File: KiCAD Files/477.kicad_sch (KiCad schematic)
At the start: 25 parts, among them IC1 W25N01GVSFIG, IC2 W25N01GVSFIG, IC3 W25N01GVSFIG, IC4 W25N01GVSFIG, J1 BM06B-SRSS-TBT_LF__SN_, J2 6364372-2

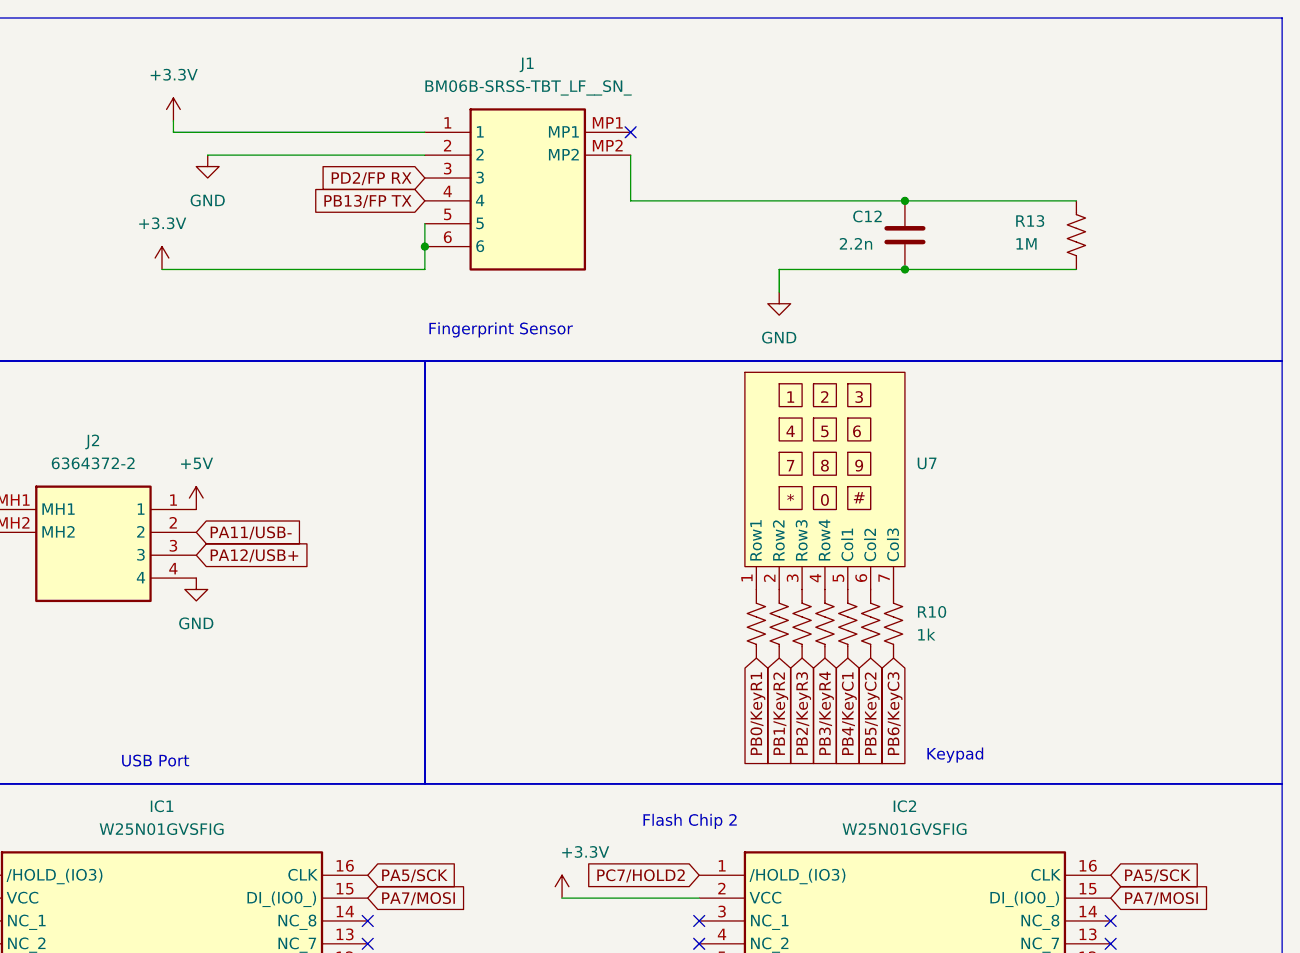
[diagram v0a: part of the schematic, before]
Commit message: added additional connector
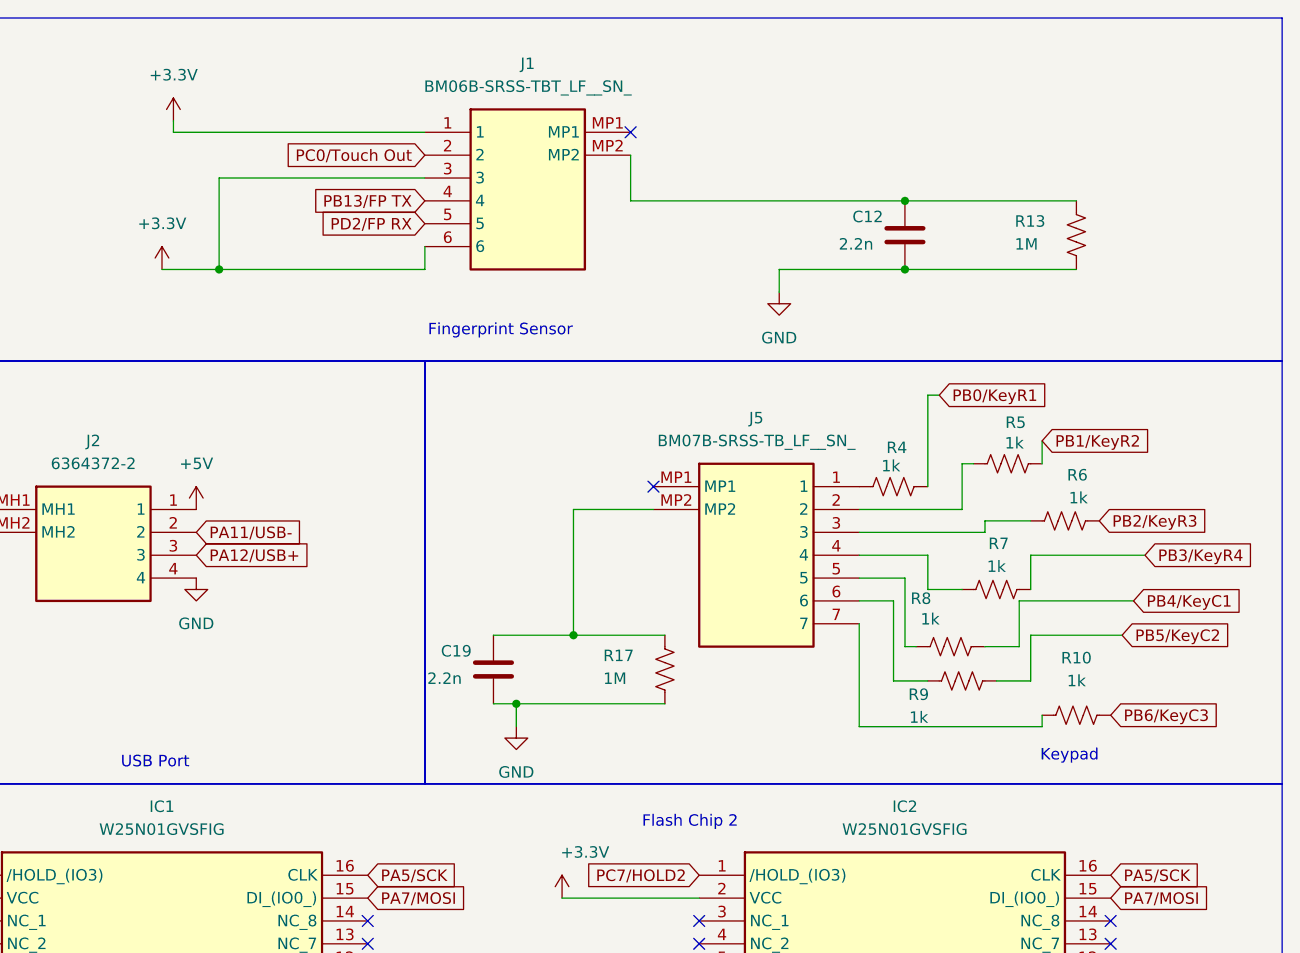
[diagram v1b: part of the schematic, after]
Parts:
- removed U7: ~, symbol CustomSymbols:keypad
- added C19: 2.2n, Capacitor_SMD:C_0805_2012Metric_Pad1.18x1.45mm_HandSolder, symbol CustomSymbols:C
- added J5: BM07B-SRSS-TB_LF__SN_, BM07BSRSSTBLFSN, symbol CustomSymbols:BM07B-SRSS-TB_LF__SN_
- added R17: 1M, Resistor_SMD:R_0805_2012Metric_Pad1.20x1.40mm_HandSolder, symbol CustomSymbols:R_US
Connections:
- net +3.3V: now also J1.3; no longer J1.5
- net GND: now also C19.2, R17.2; no longer J1.2
- net PB3/KeyR4: now also R7.1; no longer R7.2
- net PB4/KeyC1: now also R8.1; no longer R8.2
- net PB6/KeyC3: now also R10.1; no longer R10.2
- net PD2/FP RX: now also J1.5; no longer J1.3
- net at R6.1: now also J5.3
- net at R4.1: now also J5.1
- net at R5.1: now also J5.2
- net at R9.1: now also J5.6
- new net: C19.1, J5.MP2, R17.1
- new net: J5.4, R7.2
- new net: J5.5, R8.2
- new net: J5.7, R10.2
- new net PC0/Touch Out: J1.2
- no-connect marks 44 -> 45

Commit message: found final connector
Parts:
- removed DS1: WC1602A, Display:WC1602A, symbol CustomSymbols:WC1602A
- removed R12: R_US, Resistor_SMD:R_0805_2012Metric_Pad1.20x1.40mm_HandSolder, symbol CustomSymbols:R_US
- added C20: 2.2n, Capacitor_SMD:C_0805_2012Metric_Pad1.18x1.45mm_HandSolder, symbol CustomSymbols:C
- added J6: BM09B-SRSS-TB_LF__SN_, BM09BSRSSTBLFSN, symbol CustomSymbols:BM09B-SRSS-TB_LF__SN_
- R11: value R_US -> 1M
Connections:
- net +3.3V: no longer R11.1
- net +5V: now also J6.3, J6.9
- net GND: now also R11.2, C20.2, J6.1, J6.2, J6.8
- net PB10/LCD SCK: now also J6.6
- net PB12/LCD NSS: now also J6.4
- net PC1/LCD MOSI: now also J6.7
- new net: C20.1, J6.MP2, R11.1
- no-connect marks 45 -> 37
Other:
- note removed: "Revisit with specifications on LCD after part selection."

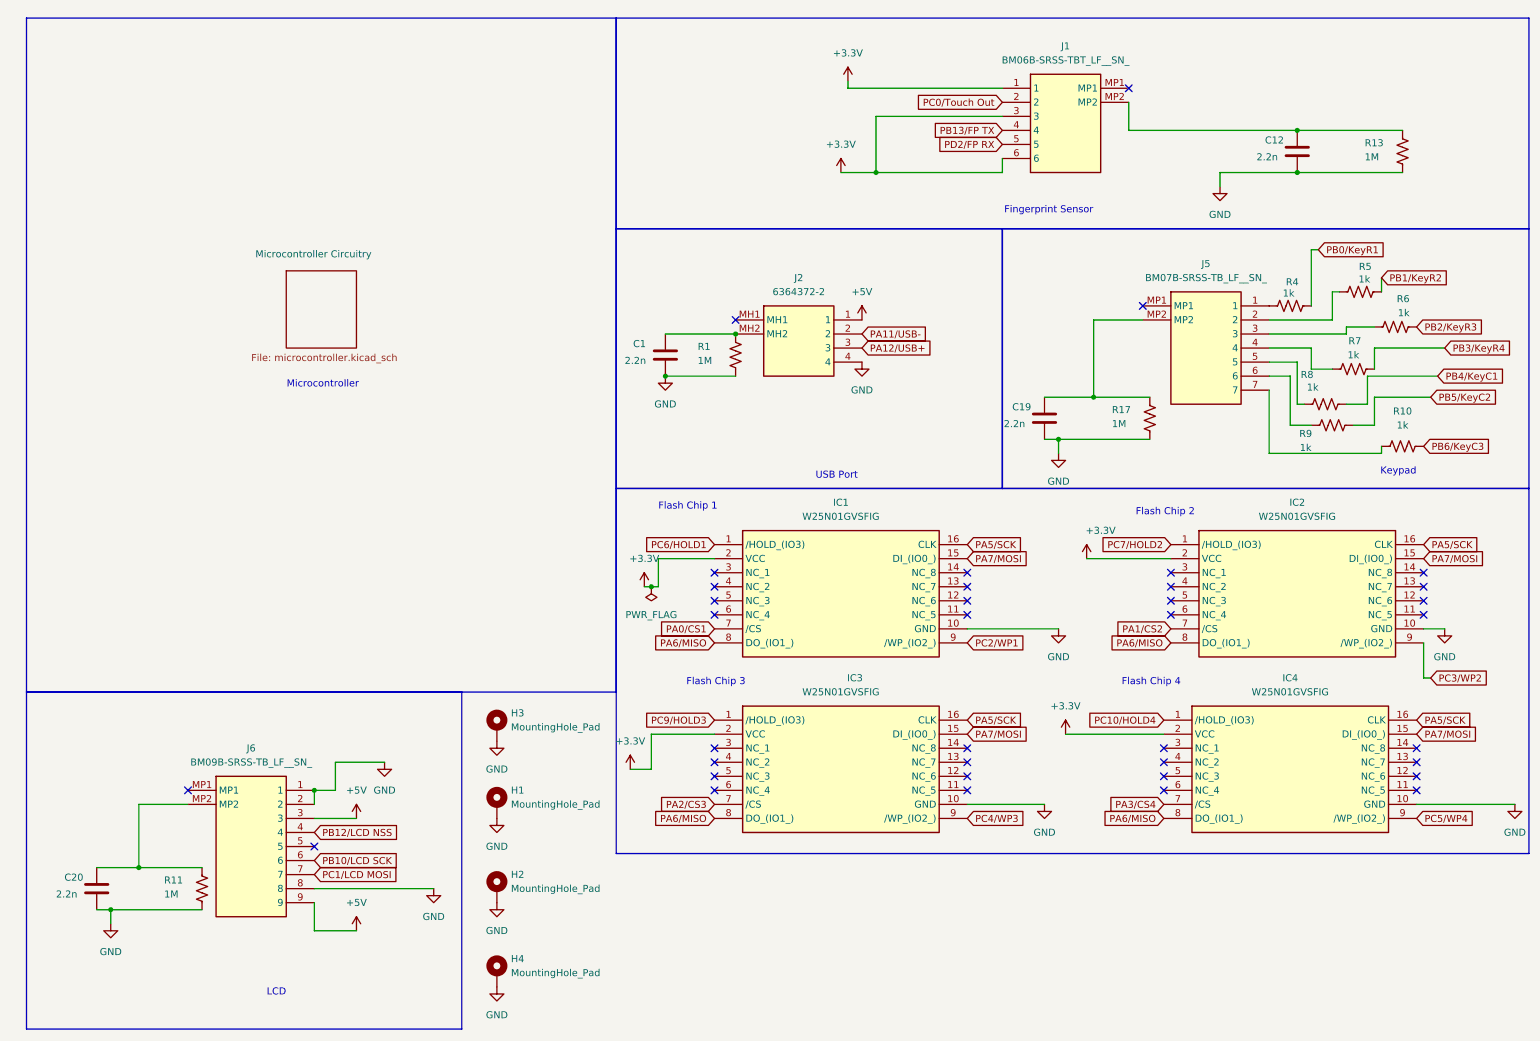
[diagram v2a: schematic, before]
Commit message: finalized schematic
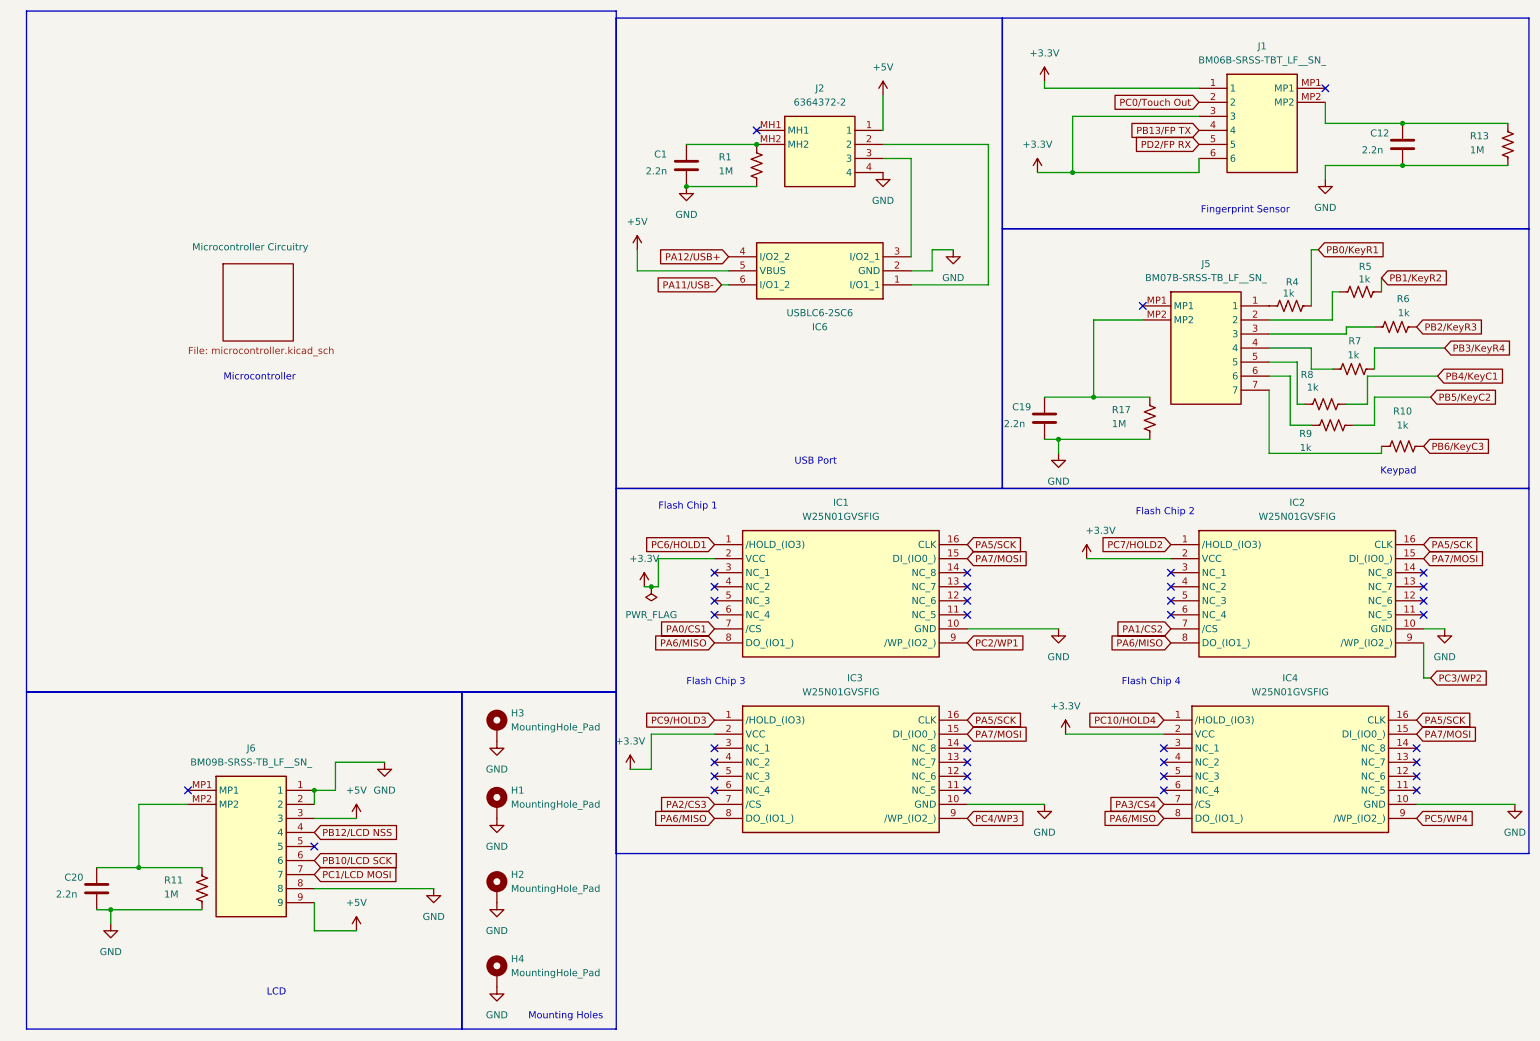
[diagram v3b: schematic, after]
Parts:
- added IC6: USBLC6-2SC6, SOT95P280X145-6N, symbol CustomSymbols:USBLC6-2SC6
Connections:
- net +5V: now also IC6.5 (VBUS)
- net GND: now also IC6.2 (GND)
- net PA11/USB-: now also IC6.6 (I/O1_2); no longer J2.2
- net PA12/USB+: now also IC6.4 (I/O2_2); no longer J2.3
- new net: IC6.1 (I/O1_1), J2.2
- new net: IC6.3 (I/O2_1), J2.3
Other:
- note added: "Mounting Holes"
- moved on the sheet: C1, C12, J1, J2, R1, R13

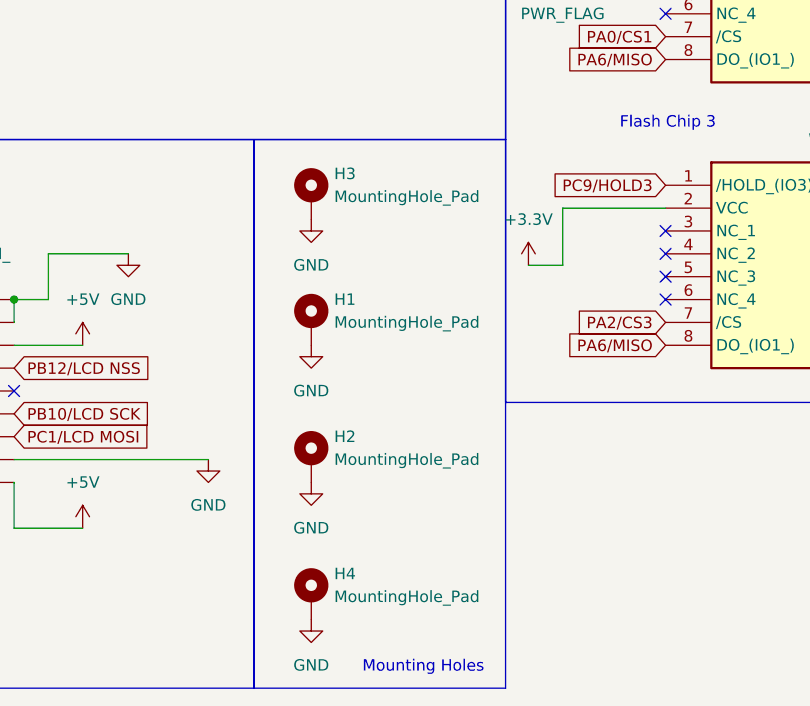
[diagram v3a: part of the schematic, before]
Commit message: modified mounting holes
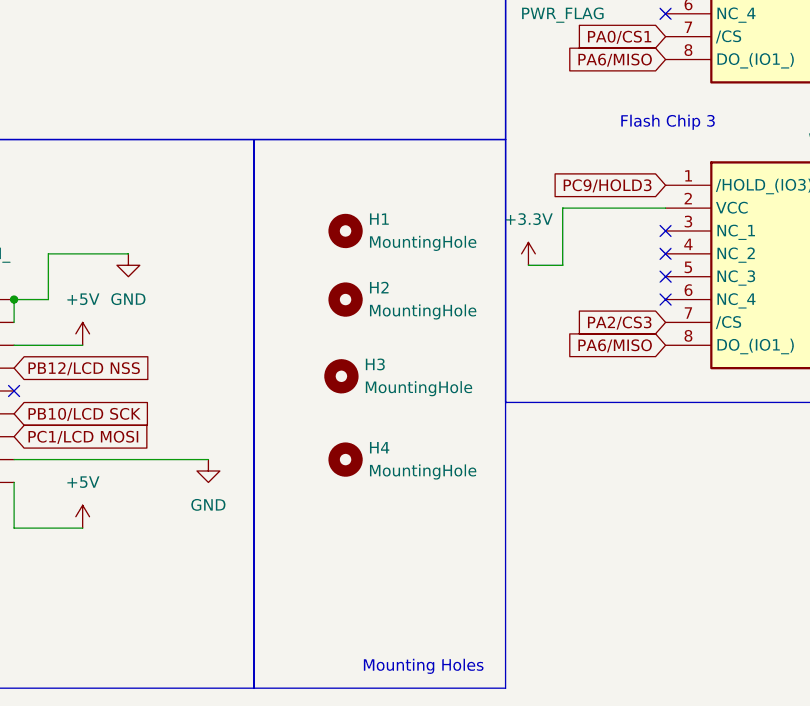
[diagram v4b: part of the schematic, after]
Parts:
- removed H1, H2, H3, H4: MountingHole_Pad, MountingHole:MountingHole_3.2mm_M3_DIN965_Pad, symbol Mechanical:MountingHole_Pad
- added H1, H2, H3, H4: MountingHole, MountingHole:MountingHole_3.2mm_M3_DIN965, symbol Mechanical:MountingHole

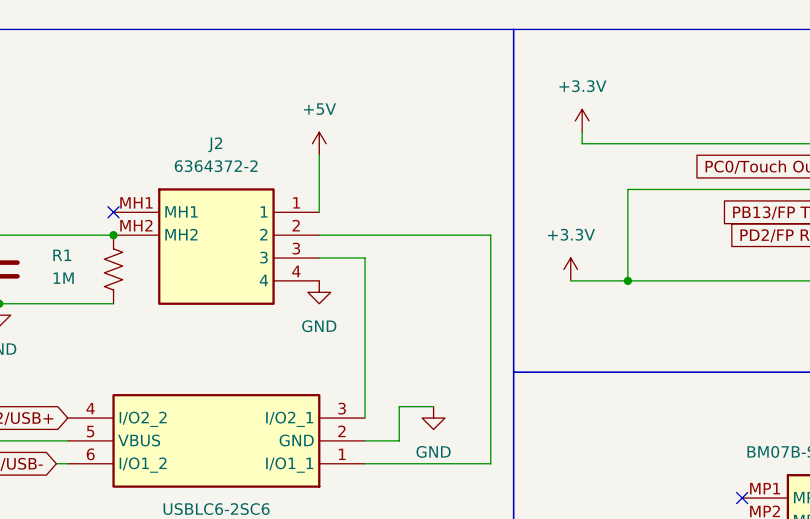
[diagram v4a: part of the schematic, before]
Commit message: updated with 3d models
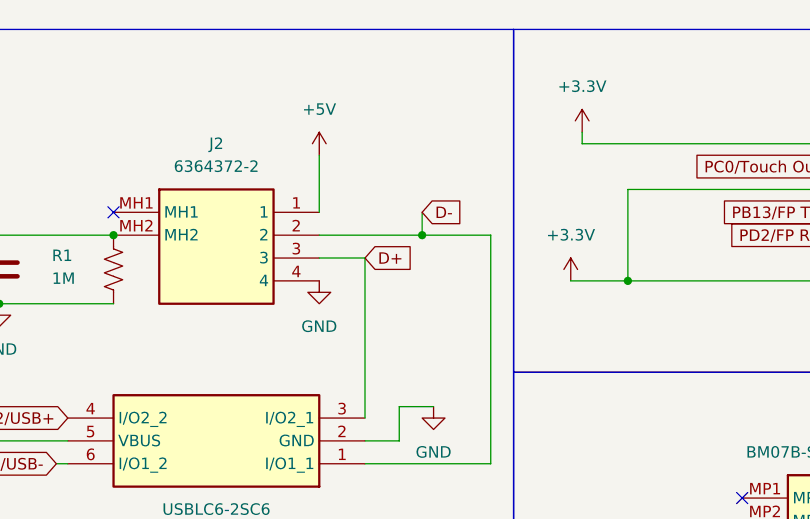
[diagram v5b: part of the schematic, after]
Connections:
- net D-: now reaches IC6.1 (I/O1_1), J2.2
- net D+: now reaches IC6.3 (I/O2_1), J2.3
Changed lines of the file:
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@@
+	)
+	(junction
+		(at 179.07 36.83)
+		(diameter 0)
+		(color 0 0 0 0)
 	)
 	(junction
@@
 	(wire
 		(pts
+			(xy 179.07 34.29) (xy 179.07 36.83)
+		)
+		(stroke
+			(width 0)
+			(type default)
+		)
+	)
+	(wire
+		(pts
 			(xy 132.08 44.45) (xy 144.78 44.45)
 		)
@@
 	(wire
 		(pts
+			(xy 179.07 36.83) (xy 186.69 36.83)
+		)
+		(stroke
+			(width 0)
+			(type default)
+		)
+	)
+	(wire
+		(pts
 			(xy 247.65 33.02) (xy 247.65 29.21)
 		)
@@
 	(wire
 		(pts
-			(xy 167.64 36.83) (xy 186.69 36.83)
+			(xy 167.64 36.83) (xy 179.07 36.83)
 		)
 		(stroke
@@
 		)
 	)
+	(global_label "D-"
+		(shape input)
+		(at 179.07 34.29 0)
+		(fields_autoplaced yes)
+		(effects
+			(font
+				(size 1.27 1.27)
+				(color 0 0 0 1)
+			)
+			(justify left)
+		)
+		(property "Intersheetrefs" "${INTERSHEET_REFS}"
+			(at 184.8976 34.29 0)
+			(effects
+				(font
+					(size 1.27 1.27)
+				)
+				(justify left)
+				(hide yes)
+			)
+		)
+	)
 	(global_label "PA7{slash}MOSI"
 		(shape input)
@@
 				(hide yes)
 			)
+		)
+	)
+	(global_label "D+"
+		(shape input)
+		(at 172.72 39.37 0)
+		(fields_autoplaced yes)
+		(effects
+			(font
+				(size 1.27 1.27)
+				(color 0 0 0 1)
+			)
+			(justify left)
+		)
+		(property "Intersheetrefs" "${INTERSHEET_REFS}"
+			(at 178.5476 39.37 0)
+			(effects
+				(font
+					(size 1.27 1.27)
+				)
+				(justify left)
+				(hide yes)
+			)
